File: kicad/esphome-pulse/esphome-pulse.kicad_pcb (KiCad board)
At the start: 2 copper layers, 26.3 x 24.7 mm, 3 parts, among them U2 PJ-320A

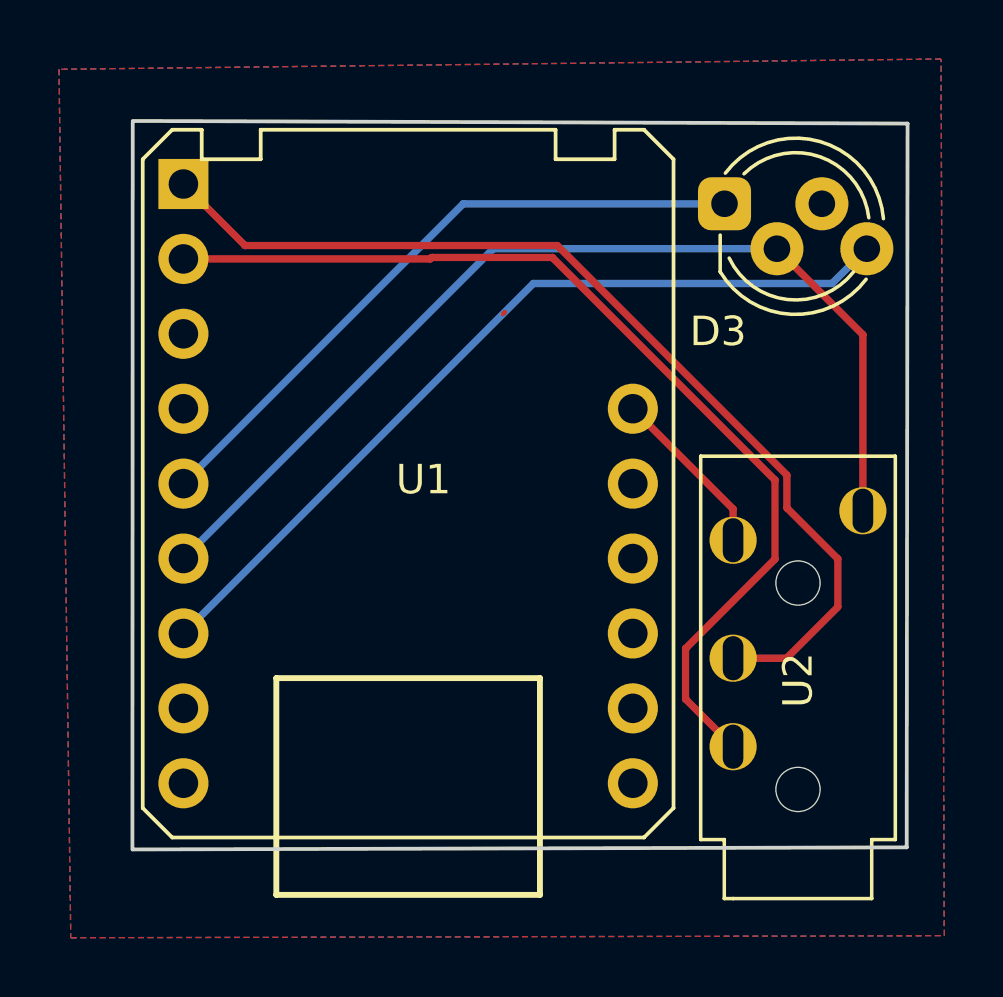
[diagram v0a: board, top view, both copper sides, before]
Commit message: Update PCB and add images to README
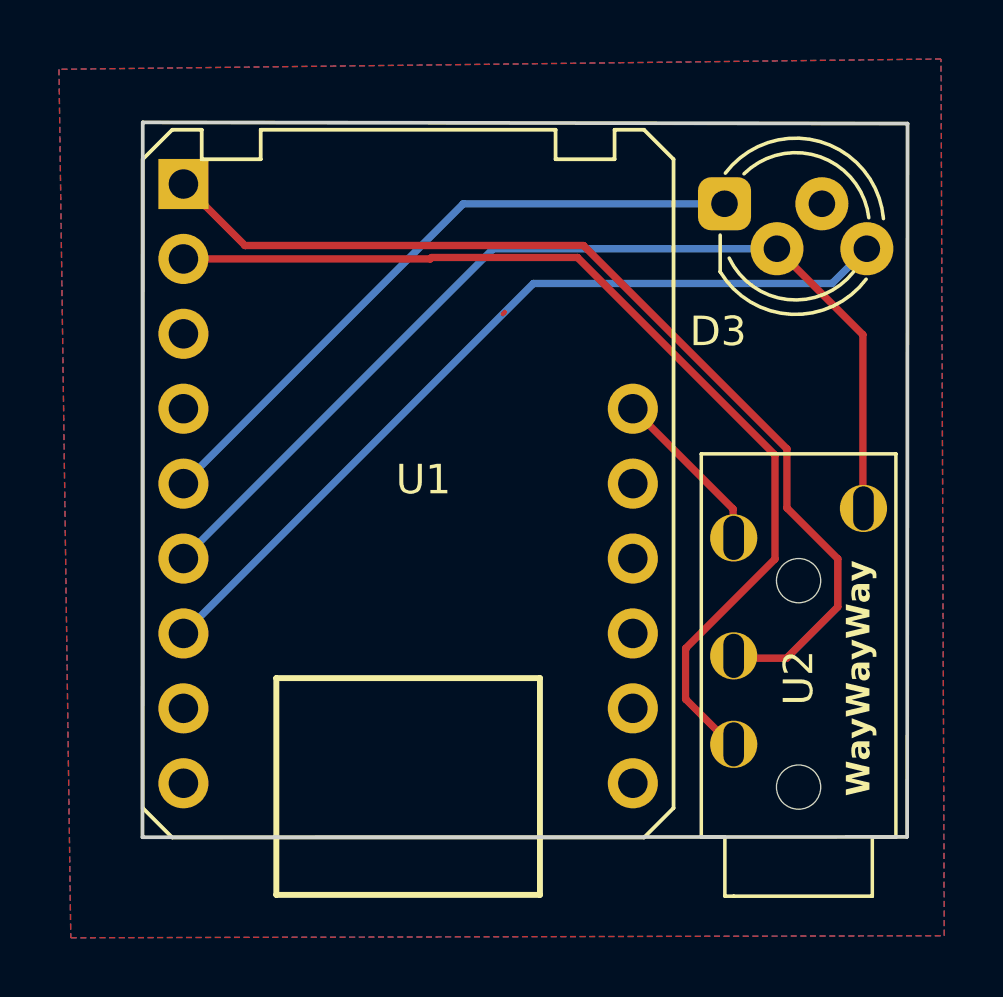
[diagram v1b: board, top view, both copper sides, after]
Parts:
- moved U2 0.08 mm to (89.8, 94.9)
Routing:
- net Net-(U1-A1CH0/TCH1/GPIO1): track 34.0 -> 34.5 mm
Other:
- board size 26.3 x 24.7 mm -> 25.9 x 24.2 mm
- board text added: "PaulSchulz esphome-pulse 18 May 2025"
- board text added: "WayWayWay"

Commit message: kicad: Close board outline cut
This error was raised in the Engineering Design Rule checks.
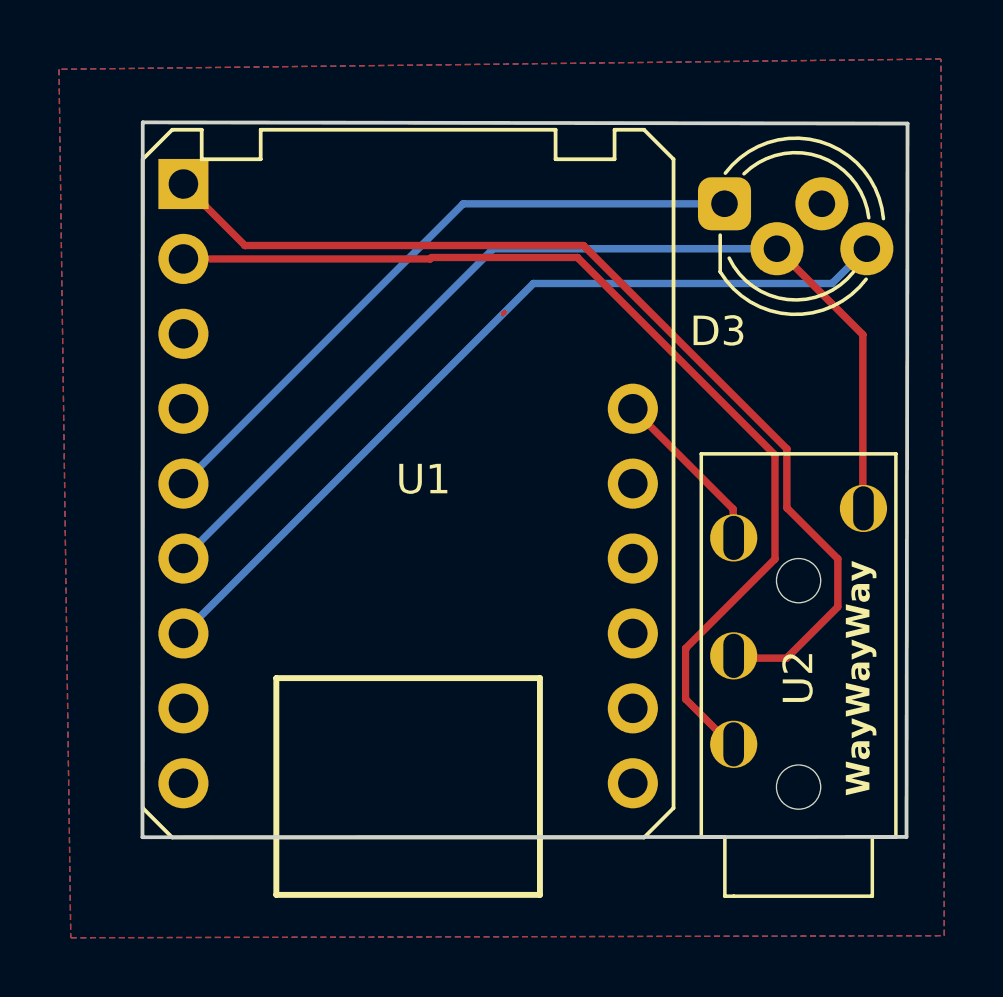
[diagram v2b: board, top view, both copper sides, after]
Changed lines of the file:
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@@
 	)
 	(gr_line
-		(start 95.674988 68.74)
+		(start 95.676889 68.740003)
 		(end 69.74 68.7)
 		(stroke
@@
 	)
 	(gr_line
-		(start 95.660056 92.93)
+		(start 95.64 92.93)
 		(end 95.674988 68.74)
 		(stroke
